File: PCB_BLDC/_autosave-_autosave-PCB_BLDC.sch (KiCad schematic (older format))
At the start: 54 parts, among them M1 Stepper_Motor_unipolar_6pin, Q1 IRF4905, SW1 Rotary_Encoder, U1 LF15_TO220, U2 BTN8962TA, U3 BTN8962TA, U4 BTN8962TA

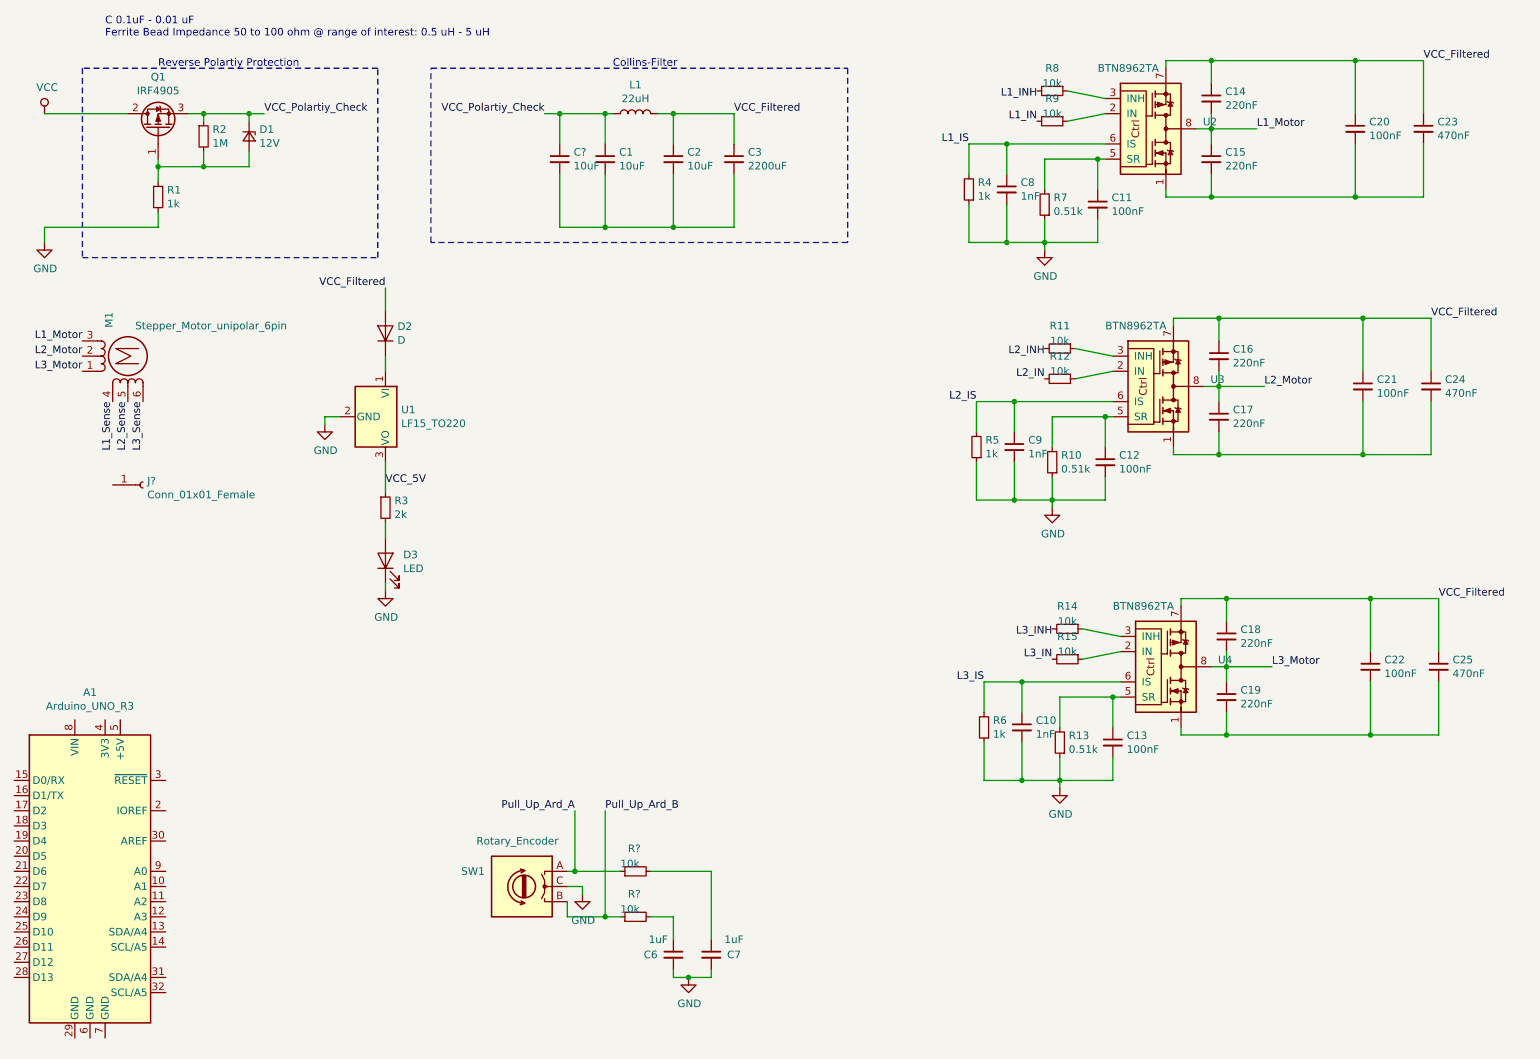
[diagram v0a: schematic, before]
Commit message: Main: Improve Schematic
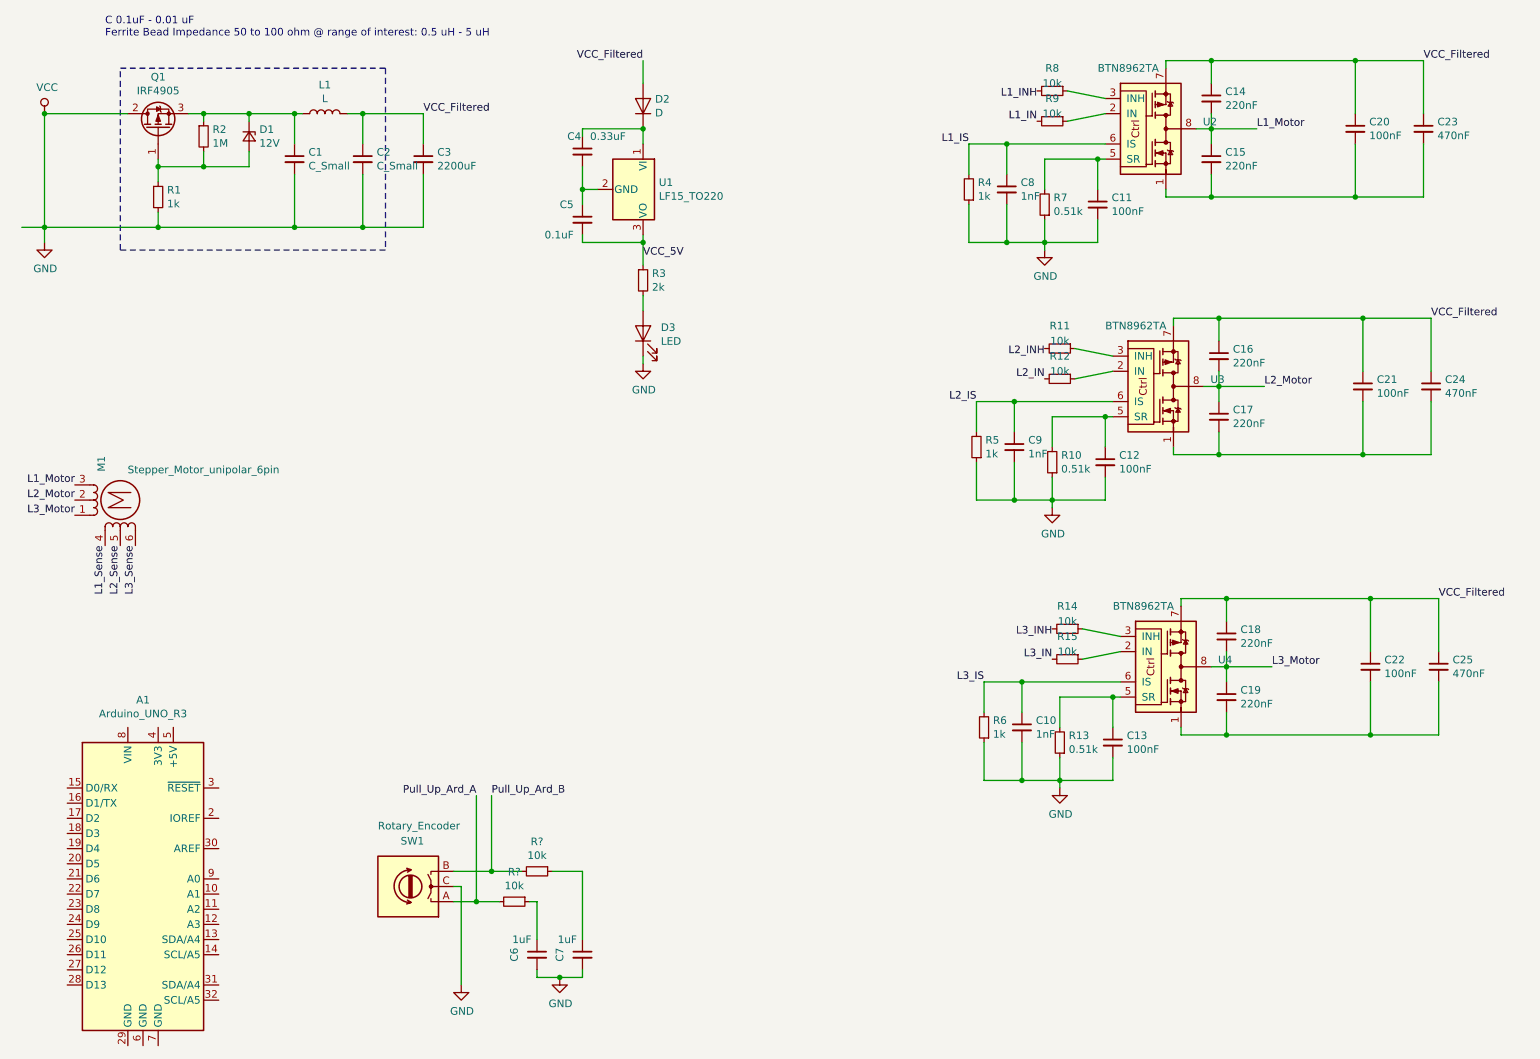
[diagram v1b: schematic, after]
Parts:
- removed C?: 10uF, symbol Device:C_Small
- removed J?: Conn_01x01_Female, symbol Connector:Conn_01x01_Female
- removed R? (x2): 10k, Resistor_SMD:R_1206_3216Metric_Pad1.30x1.75mm_HandSolder, symbol Device:R_Small
- added C4: 0.33uF, symbol Device:C_Small
- added C5: 0.1uF, symbol Device:C_Small
- added R? (x2): 10k, symbol Device:R_Small
- C1, C2: value 10uF -> C_Small
- L1: value 22uH -> L
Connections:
- net VCC is gone; now on net GND: Q1.2 (D)
- net GND: now also C1.2, C2.2, C3.2; no longer U1.2 (GND)
- net Pull_Up_Ard_A: now also R?.2
- net Pull_Up_Ard_B: now also R?.2
- net VCC_5V: now also C5.2
- net at D2.1 (K), U1.1 (VI): now also C4.1
- net at C7.1: now also R?.1
- net at C6.1: now also R?.1
- net VCC_Polartiy_Check: no longer names the net of C1.1, D1.1 (K), L1.1, Q1.3 (S), R2.1
- new net: C4.2, C5.1, U1.2 (GND)
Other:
- note removed: "Collins-Filter\n"
- note removed: "Reverse Polartiy Protection\n"
- moved on the sheet: A1, C1, C2, C3, C6, C7, D2, D3, L1, M1, R3, SW1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
